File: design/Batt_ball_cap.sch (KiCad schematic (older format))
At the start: 7 parts

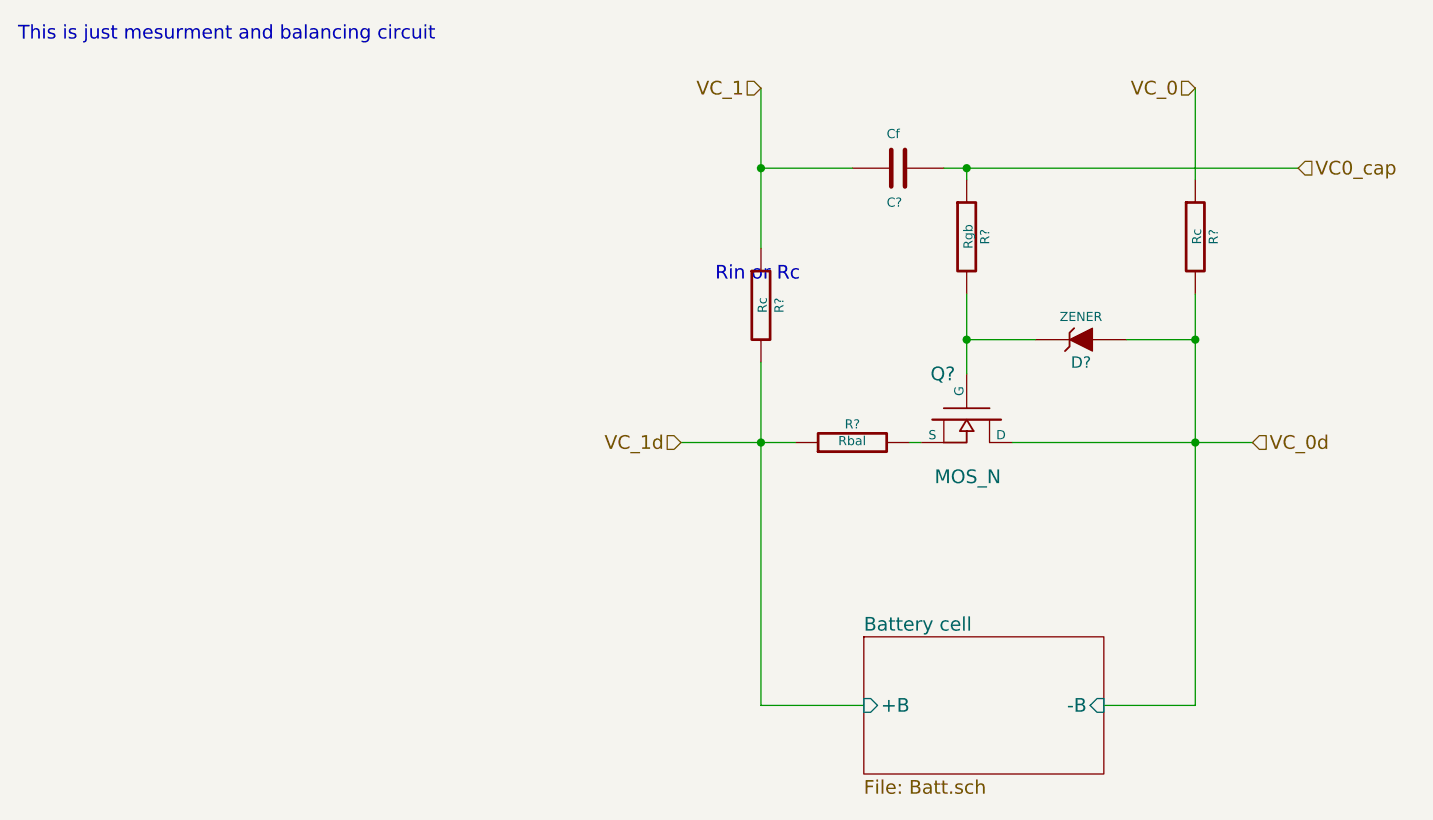
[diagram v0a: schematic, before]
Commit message: Add a cell to 10 but currently a scheme is a total mess fix it
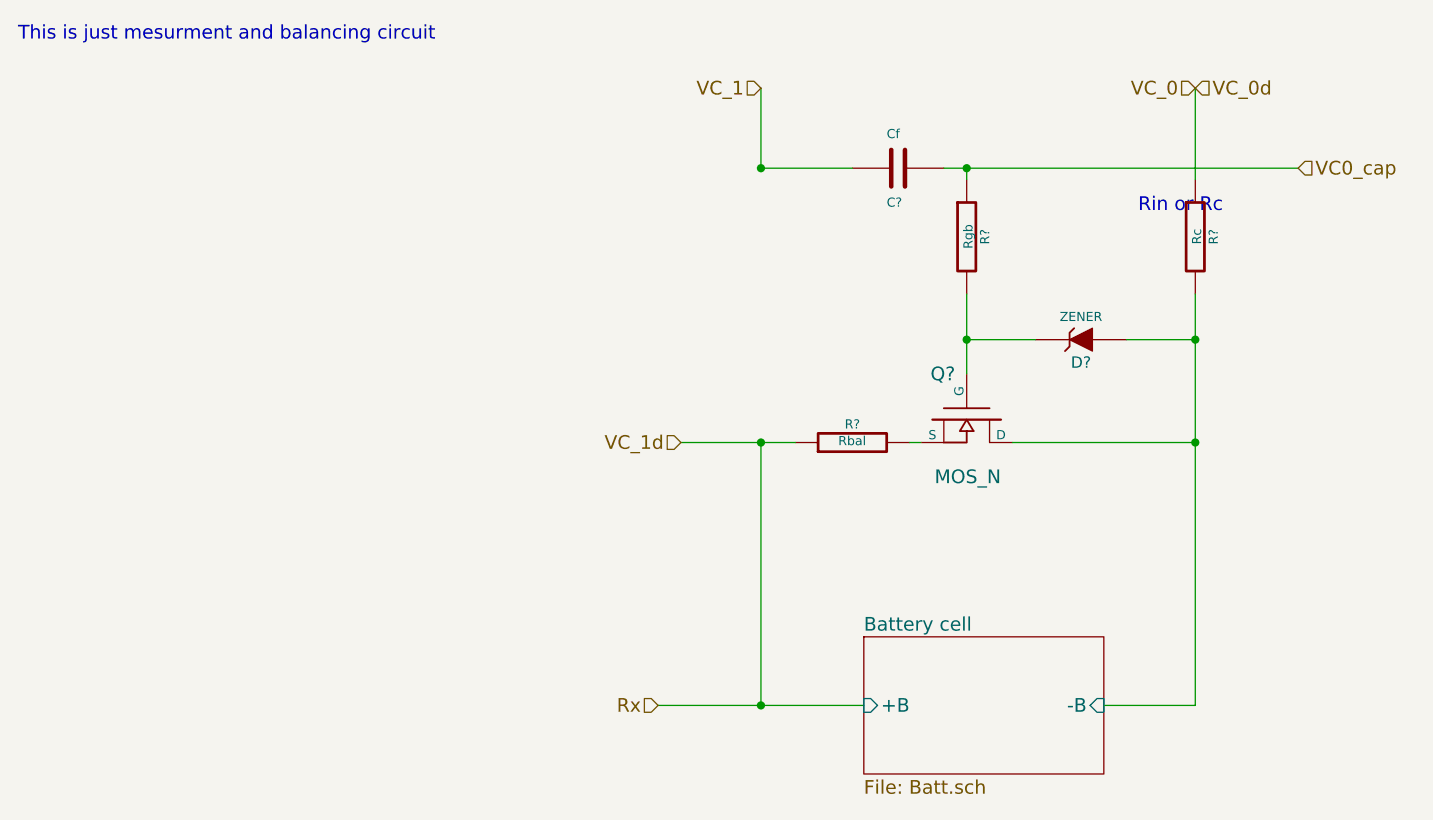
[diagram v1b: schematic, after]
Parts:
- removed R?: Rc, symbol R
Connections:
- net VC_0d renamed Battery cell/-B
- net VC_1d renamed Rx
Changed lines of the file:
@@
 $Descr A4 11693 8268
 encoding utf-8
-Sheet 7 10
+Sheet 21 30
 Title ""
 Date ""
@@
 U 1 1 55BD57AA
 P 5400 2750
+AR Path="/55BB8FBC/3A50D488/55BD57AA" Ref="Q?"  Part="1"
+AR Path="/55BB8FBC/3A51DCAC/55BD57AA" Ref="Q?"  Part="1"
 F 0 "Q?" V 5200 2700 60  0000 R CNN
 F 1 "MOS_N" V 5650 2900 60  0000 R CNN
@@
 U 1 1 55BD5928
 P 4900 2850
+AR Path="/55BB8FBC/3A50D488/55BD5928" Ref="R?"  Part="1"
+AR Path="/55BB8FBC/3A51DCAC/55BD5928" Ref="R?"  Part="1"
 F 0 "R?" V 4980 2850 40  0000 C CNN
 F 1 "Rbal" V 4907 2851 40  0000 C CNN
@@
 U 1 1 55BD5ABC
 P 5900 2400
+AR Path="/55BB8FBC/3A50D488/55BD5ABC" Ref="D?"  Part="1"
+AR Path="/55BB8FBC/3A51DCAC/55BD5ABC" Ref="D?"  Part="1"
 F 0 "D?" H 5900 2500 50  0000 C CNN
 F 1 "ZENER" H 5900 2300 40  0000 C CNN
@@
 U 1 1 55BD5B30
 P 6400 1950
+AR Path="/55BB8FBC/3A50D488/55BD5B30" Ref="R?"  Part="1"
+AR Path="/55BB8FBC/3A51DCAC/55BD5B30" Ref="R?"  Part="1"
 F 0 "R?" V 6480 1950 40  0000 C CNN
 F 1 "Rc" V 6407 1951 40  0000 C CNN
@@
 $EndComp
 $Comp
-L R R?
-U 1 1 55BD5E1E
-P 4500 2250
-F 0 "R?" V 4580 2250 40  0000 C CNN
-F 1 "Rc" V 4507 2251 40  0000 C CNN
-F 2 "" V 4430 2250 30  0000 C CNN
-F 3 "" H 4500 2250 30  0000 C CNN
-	1    4500 2250
-	1    0    0    -1
-$EndComp
-$Comp
 L C C?
 U 1 1 55BD5F3E
 P 5100 1650
+AR Path="/55BB8FBC/3A50D488/55BD5F3E" Ref="C?"  Part="1"
+AR Path="/55BB8FBC/3A51DCAC/55BD5F3E" Ref="C?"  Part="1"
 F 0 "C?" V 5250 1600 40  0000 L CNN
 F 1 "Cf" V 4950 1600 40  0000 L CNN
@@
 	0    1    1    0
 $EndComp
-Wire Wire Line
-	4500 1300 4500 2000
+$Comp
+L R R?
+U 1 1 55BD60D7
+P 5400 1950
+AR Path="/55BB8FBC/3A50D488/55BD60D7" Ref="R?"  Part="1"
+AR Path="/55BB8FBC/3A51DCAC/55BD60D7" Ref="R?"  Part="1"
+F 0 "R?" V 5480 1950 40  0000 C CNN
+F 1 "Rgb" V 5407 1951 40  0000 C CNN
+F 2 "" V 5330 1950 30  0000 C CNN
+F 3 "" H 5400 1950 30  0000 C CNN
+	1    5400 1950
+	1    0    0    -1
+$EndComp
+Text HLabel 4500 1300 0    60   Input ~ 0
+VC_1
+Text HLabel 6400 1300 0    60   Input ~ 0
+VC_0
+Text HLabel 4150 2850 0    60   Input ~ 0
+VC_1d
+Text HLabel 6400 1300 2    60   Input ~ 0
+VC_0d
+Text Notes 6150 1850 0    60   ~ 0
+Rin or Rc
+Text HLabel 6850 1650 2    60   Input ~ 0
+VC0_cap
+Text HLabel 4050 4000 0    60   Input ~ 0
+Rx
 Connection ~ 4500 2850
 Wire Wire Line
 	4150 2850 4650 2850
 Wire Wire Line
-	4500 4000 4950 4000
+	4050 4000 4950 4000
 Wire Wire Line
 	5150 2850 5200 2850
@@
 	6400 4000 6000 4000
 Wire Wire Line
-	5600 2850 6650 2850
-Wire Wire Line
 	6400 1300 6400 1700
 Wire Wire Line
 	4500 1650 4900 1650
-$Comp
-L R R?
-U 1 1 55BD60D7
-P 5400 1950
-F 0 "R?" V 5480 1950 40  0000 C CNN
-F 1 "Rgb" V 5407 1951 40  0000 C CNN
-F 2 "" V 5330 1950 30  0000 C CNN
-F 3 "" H 5400 1950 30  0000 C CNN
-	1    5400 1950
-	1    0    0    -1
-$EndComp
 Wire Wire Line
 	5400 1700 5400 1650
@@
 Connection ~ 5400 2400
 Connection ~ 4500 1650
-Text HLabel 4500 1300 0    60   Input ~ 0
-VC_1
-Text HLabel 6400 1300 0    60   Input ~ 0
-VC_0
-Text HLabel 4150 2850 0    60   Input ~ 0
-VC_1d
-Text HLabel 6650 2850 2    60   Input ~ 0
-VC_0d
-Wire Wire Line
-	4500 2500 4500 4000
 Wire Wire Line
 	6400 4000 6400 2200
-Text Notes 4300 2150 0    60   ~ 0
-Rin or Rc
-Text HLabel 6850 1650 2    60   Input ~ 0
-VC0_cap
 Wire Wire Line
 	5300 1650 6850 1650
+Connection ~ 4500 4000
+Wire Wire Line
+	5600 2850 6400 2850
+Wire Wire Line
+	4500 4000 4500 2850
+Wire Wire Line
+	4500 1300 4500 1650
 $EndSCHEMATC

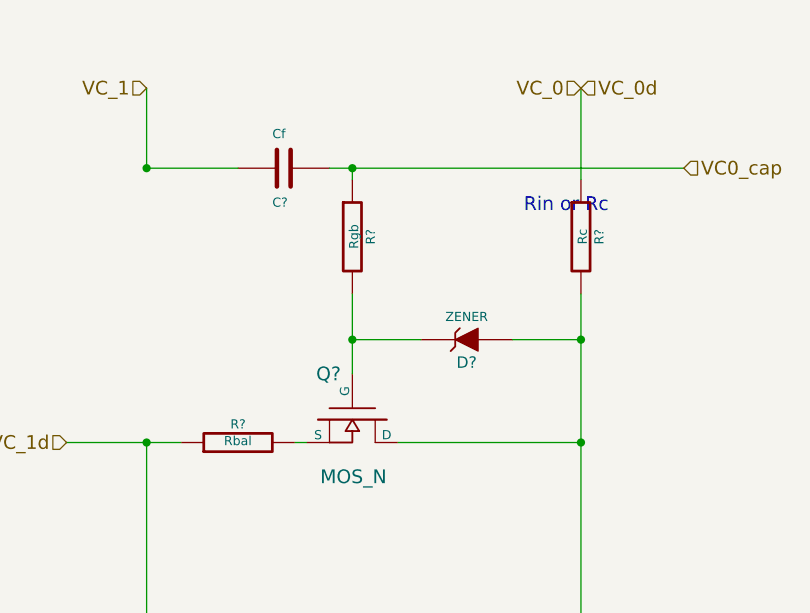
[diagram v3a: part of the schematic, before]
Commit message: Add new example in datasheet define more values
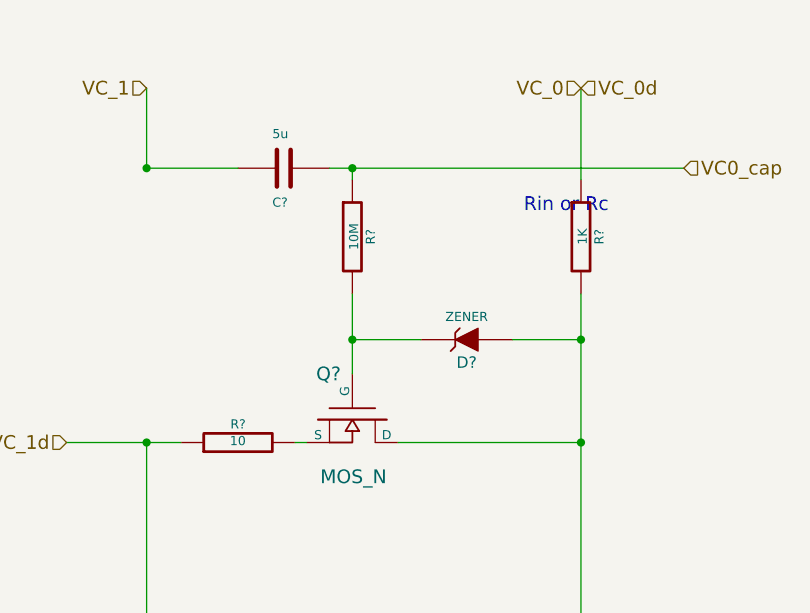
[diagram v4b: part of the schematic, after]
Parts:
- C?: value Cf -> 5u; Name (none) -> Cc
- R?: value Rbal -> 10; Name (none) -> Rbal
- R?: value Rc -> 1K
- R?: value Rgb -> 10M
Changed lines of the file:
@@
 $Descr A4 11693 8268
 encoding utf-8
-Sheet 7 101
+Sheet 18 101
 Title ""
 Date ""
@@
 AR Path="/3A58CB36/3A52C799/55BD5928" Ref="R?"  Part="1"
 F 0 "R?" V 4980 2850 40  0000 C CNN
-F 1 "Rbal" V 4907 2851 40  0000 C CNN
+F 1 "10" V 4907 2851 40  0000 C CNN
 F 2 "" V 4830 2850 30  0000 C CNN
 F 3 "" H 4900 2850 30  0000 C CNN
+F 4 "Rbal" V 4900 2850 60  0001 C CNN "Name"
 	1    4900 2850
 	0    -1   -1   0
@@
 AR Path="/3A58CB36/3A52C799/55BD5B30" Ref="R?"  Part="1"
 F 0 "R?" V 6480 1950 40  0000 C CNN
-F 1 "Rc" V 6407 1951 40  0000 C CNN
+F 1 "1K" V 6407 1951 40  0000 C CNN
 F 2 "" V 6330 1950 30  0000 C CNN
 F 3 "" H 6400 1950 30  0000 C CNN
@@
 AR Path="/3A58CB36/3A52C799/55BD5F3E" Ref="C?"  Part="1"
 F 0 "C?" V 5250 1600 40  0000 L CNN
-F 1 "Cf" V 4950 1600 40  0000 L CNN
+F 1 "5u" V 4950 1600 40  0000 L CNN
 F 2 "" H 5138 1500 30  0000 C CNN
 F 3 "" H 5100 1650 60  0000 C CNN
+F 4 "Cc" V 5100 1650 60  0001 C CNN "Name"
 	1    5100 1650
 	0    1    1    0
@@
 AR Path="/3A58CB36/3A52C799/55BD60D7" Ref="R?"  Part="1"
 F 0 "R?" V 5480 1950 40  0000 C CNN
-F 1 "Rgb" V 5407 1951 40  0000 C CNN
+F 1 "10M" V 5407 1951 40  0000 C CNN
 F 2 "" V 5330 1950 30  0000 C CNN
 F 3 "" H 5400 1950 30  0000 C CNN

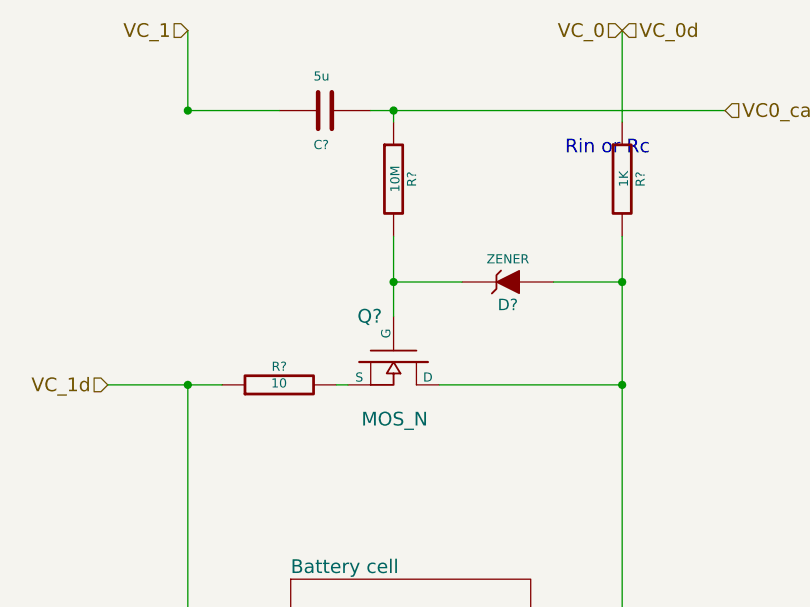
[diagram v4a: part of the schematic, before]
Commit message: Fix some schematic update pdf
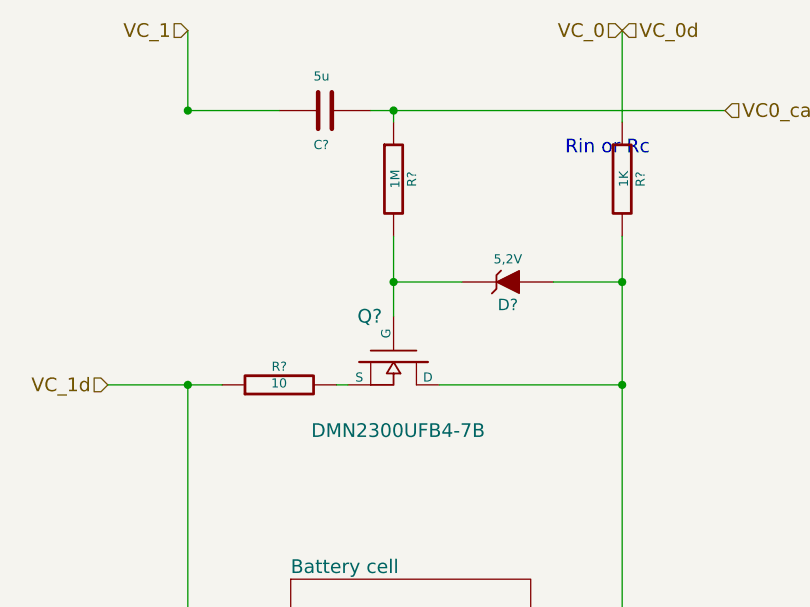
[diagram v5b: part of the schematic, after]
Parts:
- D?: value ZENER -> 5,2V
- Q?: value MOS_N -> DMN2300UFB4-7B
- R?: value 10M -> 1M
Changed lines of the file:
@@
 $Descr A4 11693 8268
 encoding utf-8
-Sheet 18 101
+Sheet 26 101
 Title ""
 Date ""
@@
 AR Path="/3A58CB36/3A51DCAC/55BD57AA" Ref="Q?"  Part="1"
 AR Path="/3A58CB36/3A52C799/55BD57AA" Ref="Q?"  Part="1"
+AR Path="/55C14E4B/3A5B5476/3A50D488/55BD57AA" Ref="Q?"  Part="1"
+AR Path="/55C14E4B/3A5B5476/3A51DCAC/55BD57AA" Ref="Q?"  Part="1"
+AR Path="/55C14E4B/3A5B5476/3A52C799/55BD57AA" Ref="Q?"  Part="1"
 F 0 "Q?" V 5200 2700 60  0000 R CNN
-F 1 "MOS_N" V 5650 2900 60  0000 R CNN
+F 1 "DMN2300UFB4-7B" V 5700 3150 60  0000 R CNN
 F 2 "" H 5400 2750 60  0000 C CNN
 F 3 "" H 5400 2750 60  0000 C CNN
@@
 AR Path="/3A58CB36/3A51DCAC/55BD5928" Ref="R?"  Part="1"
 AR Path="/3A58CB36/3A52C799/55BD5928" Ref="R?"  Part="1"
+AR Path="/55C14E4B/3A5B5476/3A50D488/55BD5928" Ref="R?"  Part="1"
+AR Path="/55C14E4B/3A5B5476/3A51DCAC/55BD5928" Ref="R?"  Part="1"
+AR Path="/55C14E4B/3A5B5476/3A52C799/55BD5928" Ref="R?"  Part="1"
 F 0 "R?" V 4980 2850 40  0000 C CNN
 F 1 "10" V 4907 2851 40  0000 C CNN
@@
 AR Path="/3A58CB36/3A51DCAC/55BD5ABC" Ref="D?"  Part="1"
 AR Path="/3A58CB36/3A52C799/55BD5ABC" Ref="D?"  Part="1"
+AR Path="/55C14E4B/3A5B5476/3A50D488/55BD5ABC" Ref="D?"  Part="1"
+AR Path="/55C14E4B/3A5B5476/3A51DCAC/55BD5ABC" Ref="D?"  Part="1"
+AR Path="/55C14E4B/3A5B5476/3A52C799/55BD5ABC" Ref="D?"  Part="1"
 F 0 "D?" H 5900 2500 50  0000 C CNN
-F 1 "ZENER" H 5900 2300 40  0000 C CNN
+F 1 "5,2V" H 5900 2300 40  0000 C CNN
 F 2 "" H 5900 2400 60  0000 C CNN
 F 3 "" H 5900 2400 60  0000 C CNN
@@
 AR Path="/3A58CB36/3A51DCAC/55BD5B30" Ref="R?"  Part="1"
 AR Path="/3A58CB36/3A52C799/55BD5B30" Ref="R?"  Part="1"
+AR Path="/55C14E4B/3A5B5476/3A50D488/55BD5B30" Ref="R?"  Part="1"
+AR Path="/55C14E4B/3A5B5476/3A51DCAC/55BD5B30" Ref="R?"  Part="1"
+AR Path="/55C14E4B/3A5B5476/3A52C799/55BD5B30" Ref="R?"  Part="1"
 F 0 "R?" V 6480 1950 40  0000 C CNN
 F 1 "1K" V 6407 1951 40  0000 C CNN
@@
 AR Path="/3A58CB36/3A51DCAC/55BD5F3E" Ref="C?"  Part="1"
 AR Path="/3A58CB36/3A52C799/55BD5F3E" Ref="C?"  Part="1"
+AR Path="/55C14E4B/3A5B5476/3A50D488/55BD5F3E" Ref="C?"  Part="1"
+AR Path="/55C14E4B/3A5B5476/3A51DCAC/55BD5F3E" Ref="C?"  Part="1"
+AR Path="/55C14E4B/3A5B5476/3A52C799/55BD5F3E" Ref="C?"  Part="1"
 F 0 "C?" V 5250 1600 40  0000 L CNN
 F 1 "5u" V 4950 1600 40  0000 L CNN
@@
 AR Path="/3A58CB36/3A51DCAC/55BD60D7" Ref="R?"  Part="1"
 AR Path="/3A58CB36/3A52C799/55BD60D7" Ref="R?"  Part="1"
+AR Path="/55C14E4B/3A5B5476/3A50D488/55BD60D7" Ref="R?"  Part="1"
+AR Path="/55C14E4B/3A5B5476/3A51DCAC/55BD60D7" Ref="R?"  Part="1"
+AR Path="/55C14E4B/3A5B5476/3A52C799/55BD60D7" Ref="R?"  Part="1"
 F 0 "R?" V 5480 1950 40  0000 C CNN
-F 1 "10M" V 5407 1951 40  0000 C CNN
+F 1 "1M" V 5407 1951 40  0000 C CNN
 F 2 "" V 5330 1950 30  0000 C CNN
 F 3 "" H 5400 1950 30  0000 C CNN
